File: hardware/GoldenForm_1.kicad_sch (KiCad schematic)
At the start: 37 parts, among them IC1 UVLO, J1 SD_Socket, J2 USB_C_Receptacle_USB2.0_14P, J3 Conn_01x04_Pin, M3 MountingHole x 4, SW1 BOOT, SW2 RESET, U1 Buck_Boost, U2 BNO055, U4 ESP32-S3-WROOM-1

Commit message: 3 ERC warnings now
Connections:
- net +3.3V renamed V_DD
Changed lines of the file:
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@@
 	)
 	(junction
-		(at 100.33 153.67)
+		(at 95.25 82.55)
 		(diameter 0)
 		(color 0 0 0 0)
 	)
 	(junction
-		(at 95.25 82.55)
+		(at 100.33 153.67)
 		(diameter 0)
 		(color 0 0 0 0)
@@
 	(wire
 		(pts
-			(xy 100.33 149.86) (xy 100.33 153.67)
-		)
-		(stroke
-			(width 0)
-			(type default)
-		)
-	)
-	(wire
-		(pts
 			(xy 121.92 69.85) (xy 128.27 69.85)
 		)
@@
 	(wire
 		(pts
+			(xy 100.33 153.67) (xy 99.06 153.67)
+		)
+		(stroke
+			(width 0)
+			(type default)
+		)
+	)
+	(wire
+		(pts
 			(xy 236.22 118.11) (xy 231.14 118.11)
 		)
@@
 	(wire
 		(pts
-			(xy 100.33 153.67) (xy 104.14 153.67)
-		)
-		(stroke
-			(width 0)
-			(type default)
-		)
-	)
-	(wire
-		(pts
 			(xy 158.75 82.55) (xy 162.56 82.55)
 		)
@@
 	(wire
 		(pts
-			(xy 63.5 86.36) (xy 63.5 88.9)
+			(xy 104.14 153.67) (xy 100.33 153.67)
 		)
 		(stroke
@@
 	(wire
 		(pts
-			(xy 96.52 171.45) (xy 96.52 173.99)
+			(xy 63.5 86.36) (xy 63.5 88.9)
 		)
 		(stroke
@@
 	(wire
 		(pts
-			(xy 121.92 72.39) (xy 128.27 72.39)
+			(xy 96.52 171.45) (xy 96.52 173.99)
 		)
 		(stroke
@@
 	(wire
 		(pts
-			(xy 99.06 153.67) (xy 100.33 153.67)
+			(xy 121.92 72.39) (xy 128.27 72.39)
 		)
 		(stroke
@@
 	(global_label "V_DD"
 		(shape input)
+		(at 104.14 153.67 0)
+		(fields_autoplaced yes)
+		(effects
+			(font
+				(size 1.27 1.27)
+			)
+			(justify left)
+		)
+		(property "Intersheetrefs" "${INTERSHEET_REFS}"
+			(at 111.7214 153.67 0)
+			(effects
+				(font
+					(size 1.27 1.27)
+				)
+				(justify left)
+				(hide yes)
+			)
+		)
+	)
+	(global_label "V_DD"
+		(shape input)
 		(at 228.6 29.21 90)
 		(fields_autoplaced yes)
@@
 		)
 	)
-	(global_label "V_DD"
-		(shape input)
-		(at 104.14 153.67 0)
-		(fields_autoplaced yes)
-		(effects
-			(font
-				(size 1.27 1.27)
-			)
-			(justify left)
-		)
-		(property "Intersheetrefs" "${INTERSHEET_REFS}"
-			(at 111.7214 153.67 0)
-			(effects
-				(font
-					(size 1.27 1.27)
-				)
-				(justify left)
-				(hide yes)
-			)
-		)
-	)
 	(global_label "V_Bat"
 		(shape input)
@@
 					(unit 1)
 				)
-			)
-		)
-	)
-	(symbol
-		(lib_id "power:+3.3V")
-		(at 100.33 149.86 0)
-		(unit 1)
-		(exclude_from_sim no)
-		(in_bom yes)
-		(on_board yes)
-		(dnp no)
-		(fields_autoplaced yes)
-		(property "Reference" "#PWR012"
-			(at 100.33 153.67 0)
-			(effects
-				(font
-					(size 1.27 1.27)
-				)
-				(hide yes)
-			)
-		)
-		(property "Value" "+3.3V"
-			(at 100.33 144.78 0)
-			(effects
-				(font
-					(size 1.27 1.27)
-				)
-			)
-		)
-		(property "Footprint" ""
-			(at 100.33 149.86 0)
-			(effects
-				(font
-					(size 1.27 1.27)
-				)
-				(hide yes)
-			)
-		)
-		(property "Datasheet" ""
-			(at 100.33 149.86 0)
-			(effects
-				(font
-					(size 1.27 1.27)
-				)
-				(hide yes)
-			)
-		)
-		(property "Description" "Power symbol creates a global label with name \"+3.3V\""
-			(at 100.33 149.86 0)
-			(effects
-				(font
-					(size 1.27 1.27)
-				)
-				(hide yes)
-			)
-		)
-		(pin "1"
-		)
-		(instances
-			(project ""
-				(path "/64cfd788-f968-4e49-826d-6322743ab44f"
-					(reference "#PWR012")
-					(unit 1)
-				)

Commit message: oops renamed to LED_2
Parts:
- D5: value LED_1 -> LED_2
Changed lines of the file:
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@@
 			)
 		)
-		(property "Value" "LED_1"
+		(property "Value" "LED_2"
 			(at 106.6165 57.404 0)
 			(effects

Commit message: some updates to footprints, USBC, buck boost, switch
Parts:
- removed C1: 20uF, Capacitor_SMD:C_0805_2012Metric_Pad1.18x1.45mm_HandSolder, symbol Device:C
- removed C2: 10uF, Capacitor_SMD:C_0805_2012Metric_Pad1.18x1.45mm_HandSolder, symbol Device:C
- removed J2: USB_C_Receptacle_USB2.0_14P, Connector_USB:USB_C_Receptacle_GCT_USB4135-GF-A_6P_TopMnt_Horizontal, symbol Connector:USB_C_Receptacle_USB2.0_14P
- removed L2: SRP5030T-2R2M, MyFootprints:INDM5752X300N, symbol MySymbols:SRP5030T-2R2M
- removed U1: Buck_Boost, MyFootprints:SON50P250X250X80-11N, symbol MySymbols:RT6150B-33GQW
- added C10: 47uF, symbol Device:C
- added C9: 22uF, symbol Device:C
- added D6: VBUS_LED, symbol Device:LED
- added J4: USB4105-GF-A, USB4105_GCT, symbol MySymbols:USB4105-GF-A
- added R14, R15: 5.1k, symbol Device:R_US
- added R16: 91k, symbol Device:R_US
- added S1: SLW-1276864-4A-D, SLW12768644AD, symbol MySymbols:SLW-1276864-4A-D
- added U3: Buck_Boost, MICROSIP8_SIU_TEX, symbol MySymbols:TPSM83100SIUR
- R5: value 5.1k -> 1k
- R6: value 5.1k -> 511k
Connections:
- net D+: now also J4.A6 (DP1), J4.B6 (DP2)
- net D-: now also J4.A7 (DN1), J4.B7 (DN2)
- net GND: now also C10.2, C9.2, D6.1 (K), J4.A1-B12 (GND), J4.B1-A12 (GND), R14.2, R15.1, R16.2, S1.1 (NC), U3.2 (GND), U3.3 (GND), U3.6 (GND); no longer R5.2, R6.2
- net V_Bat: now also C9.1, U3.1 (VIN)
- net V_DD: now also R6.1, C10.1, U3.4 (VOUT), U3.7 (MODE)
- net at R5.1: now also D6.2 (A)
- net UVLO_EN: now reaches IC1.1 (~{RESET}), R1.2
- net UVLO_EN: now also S1.3 (NO)
- new net: J4.A5 (CC1), R15.2
- new net: R16.1, R6.2, U3.5 (FB)
- new net: J4.B4-A9 (VBUS), R5.2
- new net: J4.B5 (CC2), R14.1
- new net BUCK_EN: S1.2 (COM), U3.8 (EN)
- new net V_BUS: J4.A4-B9 (VBUS)
- no-connect marks 14 -> 16
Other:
- note added: "USB C"

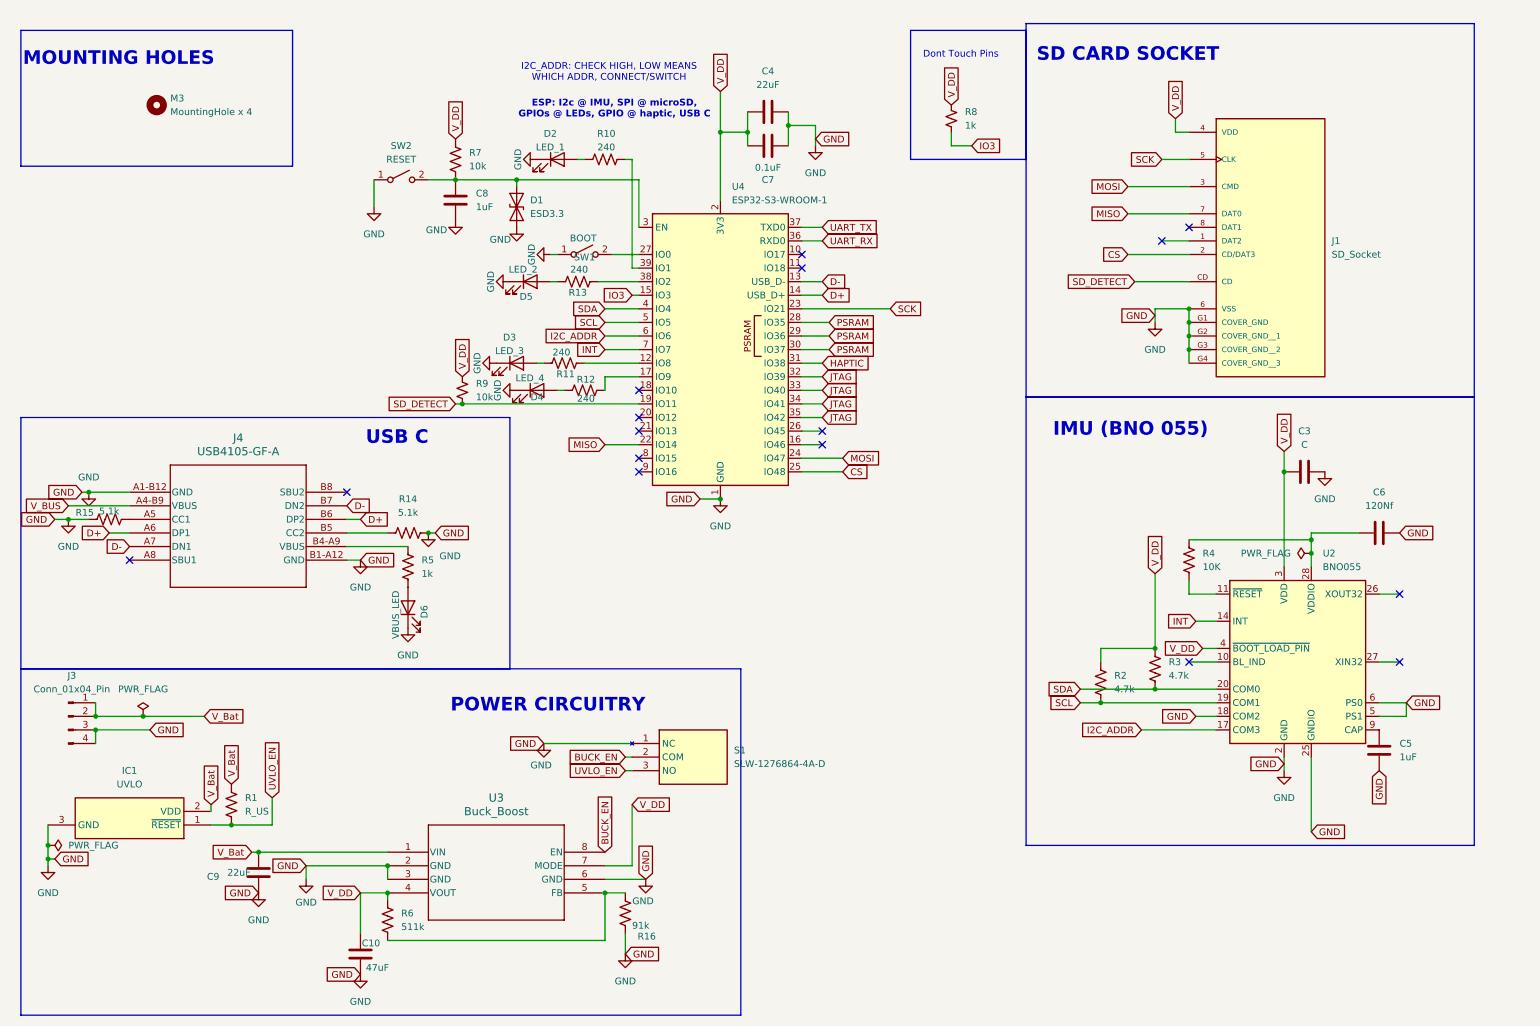
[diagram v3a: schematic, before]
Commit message: added new sd card socket, esd protection for boot and en, uart debug
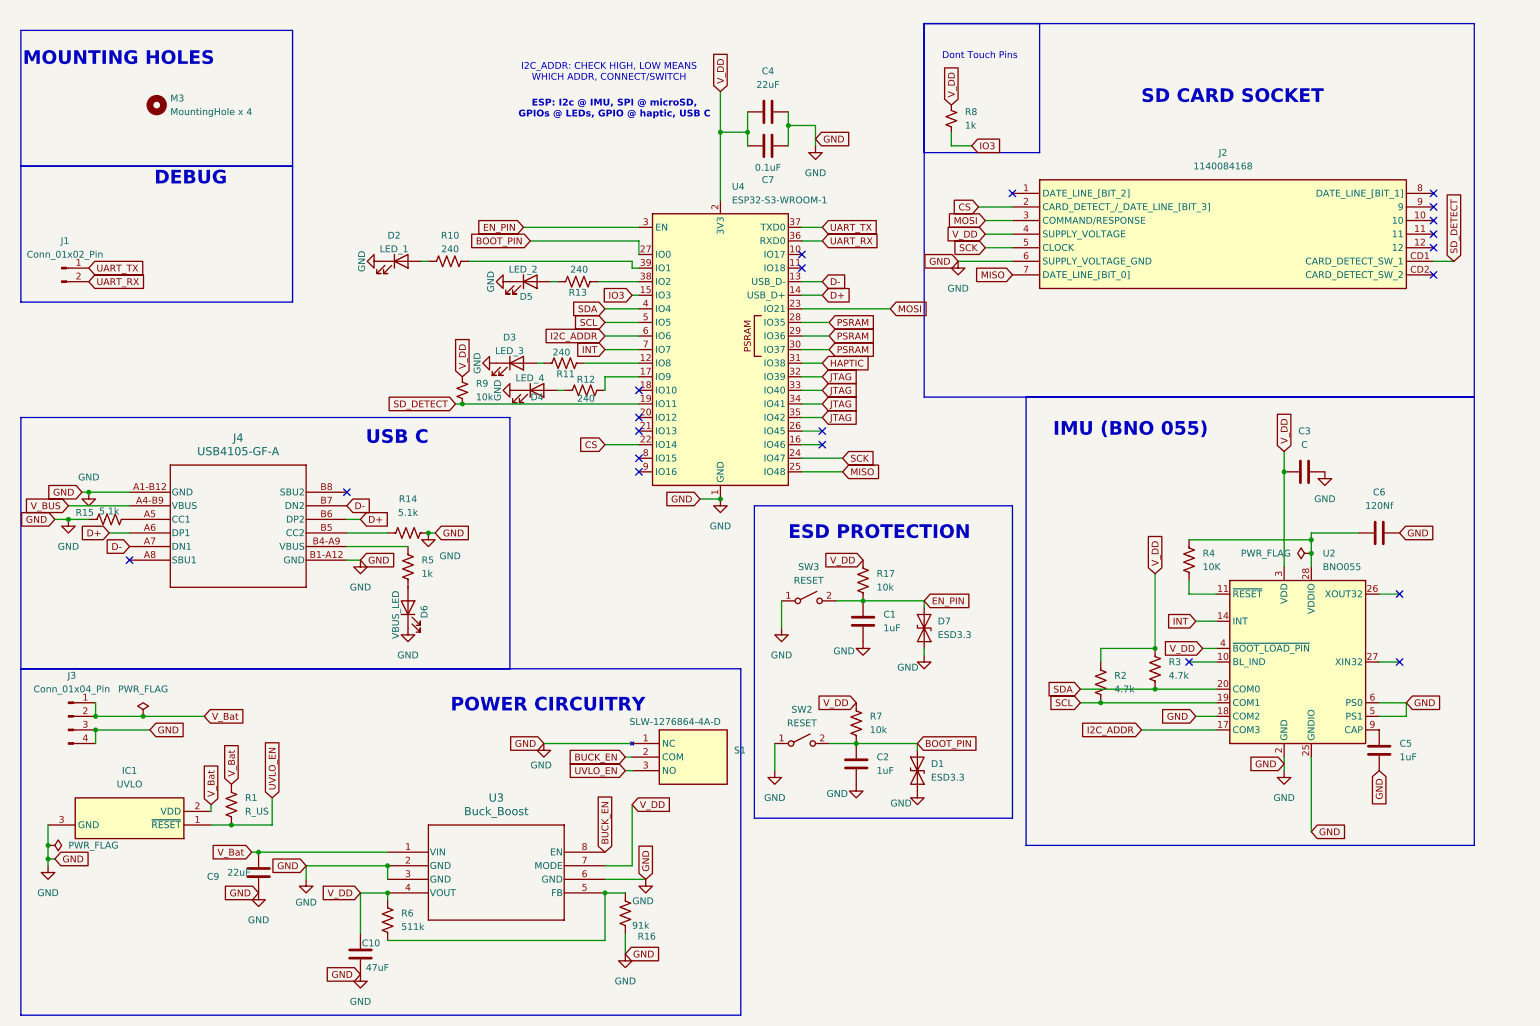
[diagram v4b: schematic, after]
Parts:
- removed C8: 1uF, symbol Device:C
- removed J1: SD_Socket, MyFootprints:CUI_MSD-4-A, symbol MySymbols:MSD-4-A
- removed SW1: BOOT, symbol Switch:SW_SPST
- added C1, C2: 1uF, symbol Device:C
- added D7: ESD3.3, Diode_SMD:D_SOD-923, symbol Diode:ESD9B3.3ST5G
- added J1: Conn_01x02_Pin, Connector_PinHeader_1.00mm:PinHeader_1x02_P1.00mm_Vertical, symbol Connector:Conn_01x02_Pin
- added J2: 1140084168, MyFootprints:1140084168, symbol MySymbols:1140084168
- added R17: 10k, symbol Device:R_US
- added SW3: RESET, symbol Switch:SW_SPST
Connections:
- net CS: now also U4.22 (IO14), J2.2 (CARD_DETECT_/_DATE_LINE_[BIT_3]); no longer U4.25 (IO48)
- net GND: now also C1.2, C2.2, D7.1 (A1), J2.6 (SUPPLY_VOLTAGE_GND), SW3.1 (A)
- net MISO: now also U4.25 (IO48), J2.7 (DATE_LINE_[BIT_0]); no longer U4.22 (IO14)
- net MOSI: now also U4.23 (IO21), J2.3 (COMMAND/RESPONSE); no longer U4.24 (IO47)
- net SCK: now also U4.24 (IO47), J2.5 (CLOCK); no longer U4.23 (IO21)
- net SD_DETECT: now also J2.CD1 (CARD_DETECT_SW_1)
- net UART_RX: now also J1.2 (Pin_2)
- net UART_TX: now also J1.1 (Pin_1)
- net V_DD: now also J2.4 (SUPPLY_VOLTAGE), R17.1
- net BOOT_PIN: now reaches U4.27 (IO0)
- net BOOT_PIN: now also D1.2 (A2), R7.2, SW2.2 (B), C2.1
- new net EN_PIN: C1.1, D7.2 (A2), R17.2, SW3.2 (B), U4.3 (EN)
- no-connect marks 16 -> 21
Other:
- note added: "DEBUG"
- note added: "ESD PROTECTION"
- moved on the sheet: D2, R10

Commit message: added switch, led footprints
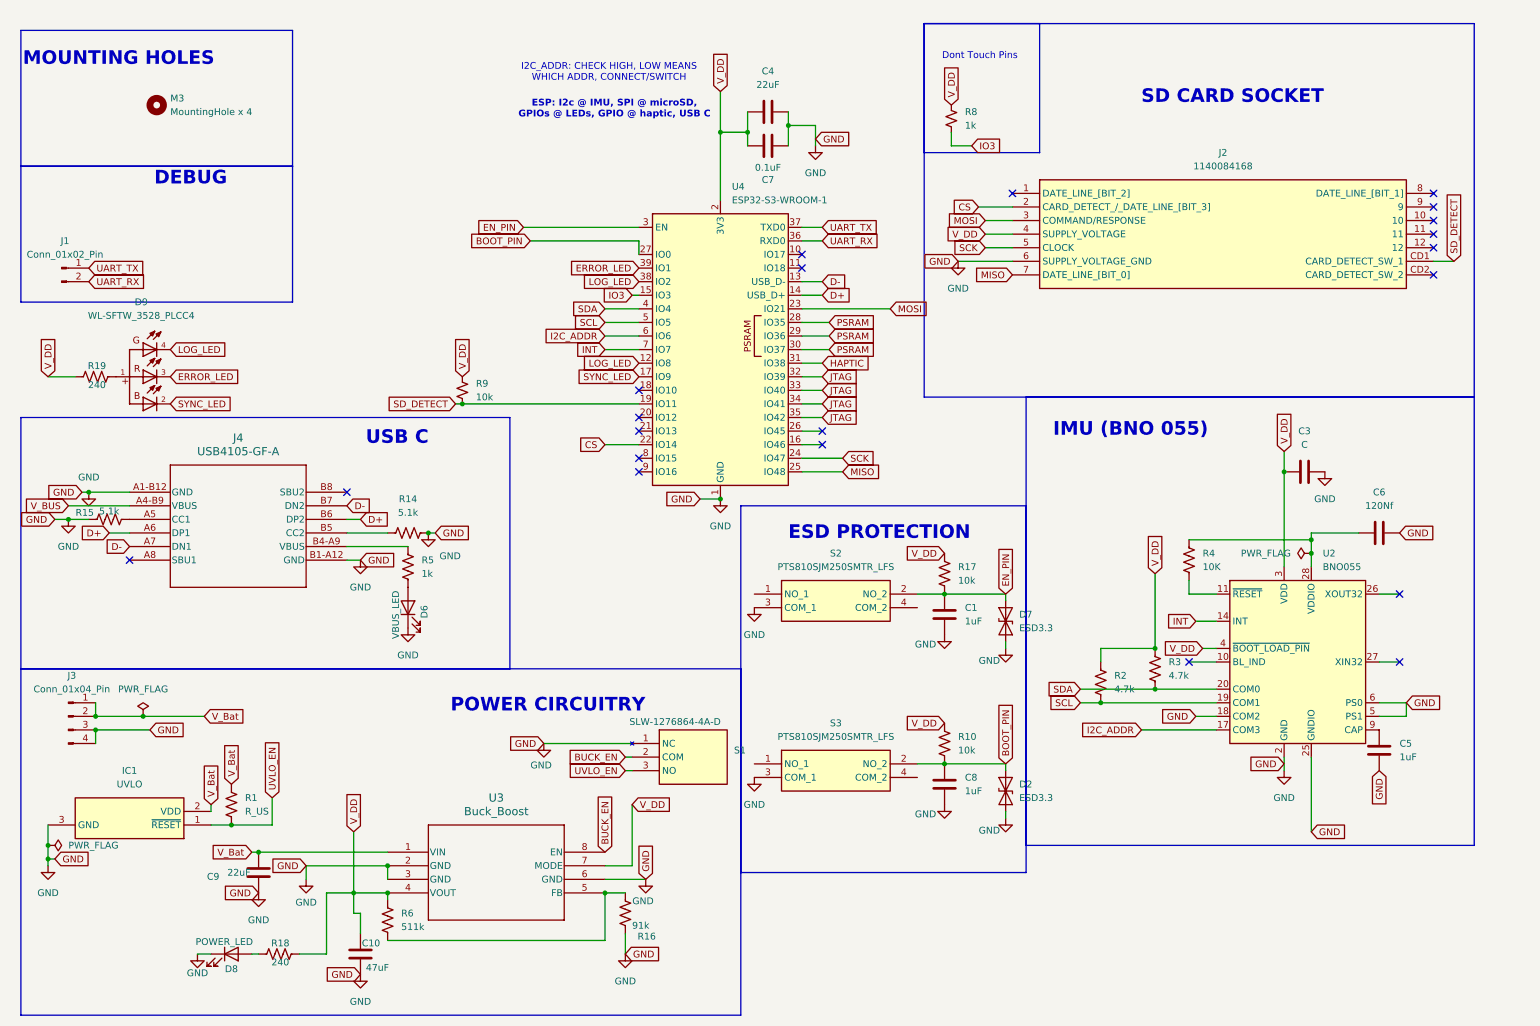
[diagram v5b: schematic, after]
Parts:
- removed C2: 1uF, symbol Device:C
- removed D1: ESD3.3, Diode_SMD:D_SOD-923, symbol Diode:ESD9B3.3ST5G
- removed D2: LED_1, symbol Device:LED
- removed D3: LED_3, symbol Device:LED
- removed D4: LED_4, symbol Device:LED
- removed D5: LED_2, symbol Device:LED
- removed R11, R12, R13: 240, symbol Device:R_US
- removed R7: 10k, symbol Device:R_US
- removed SW2, SW3: RESET, symbol Switch:SW_SPST
- added C8: 1uF, symbol Device:C
- added D2: ESD3.3, Diode_SMD:D_SOD-923, symbol Diode:ESD9B3.3ST5G
- added D8: POWER_LED, symbol Device:LED
- added D9: WL-SFTW_3528_PLCC4, MyFootprints:WL-SFTW_3528_PLCC4, symbol MySymbols:WL-SFTW_3528_PLCC4
- added R18, R19: 240, symbol Device:R_US
- added S2, S3: PTS810SJM250SMTR_LFS, MyFootprints:PTS810SJM250SMTRLFS, symbol MySymbols:PTS810SJM250SMTR_LFS
- R10: value 240 -> 10k
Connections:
- net BOOT_PIN: now also R10.2, C8.1, D2.2 (A2), S3.2 (NO_2)
- net EN_PIN: now also S2.2 (NO_2)
- net GND: now also C8.2, D2.1 (A1), D8.1 (K), S2.3 (COM_1), S3.3 (COM_1)
- net V_DD: now also R10.1, R18.2, R19.1
- net SYNC_LED: now reaches U4.17 (IO9)
- net SYNC_LED: now also D9.2
- net LOG_LED: now reaches U4.12 (IO8)
- net LOG_LED: now also U4.38 (IO2), D9.4
- net ERROR_LED: now reaches U4.39 (IO1)
- net ERROR_LED: now also D9.3; no longer R10.2
- new net: D9.1, R19.2
- new net: D8.2 (A), R18.1
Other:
- moved on the sheet: C1, D7, R17
